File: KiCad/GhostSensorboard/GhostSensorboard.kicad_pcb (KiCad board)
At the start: 2 copper layers, 50 x 50 mm, 43 parts, among them P4 CONN_02X30, Q1 BSS138, Q2 BSS138, SW1 SW_Push, U1 TCA9548ARGER, U10 GP2Y0E02B, U11 GP2Y0E02B, U12 GP2Y0E02B, U13 INA219, U2 GP2Y0E02B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

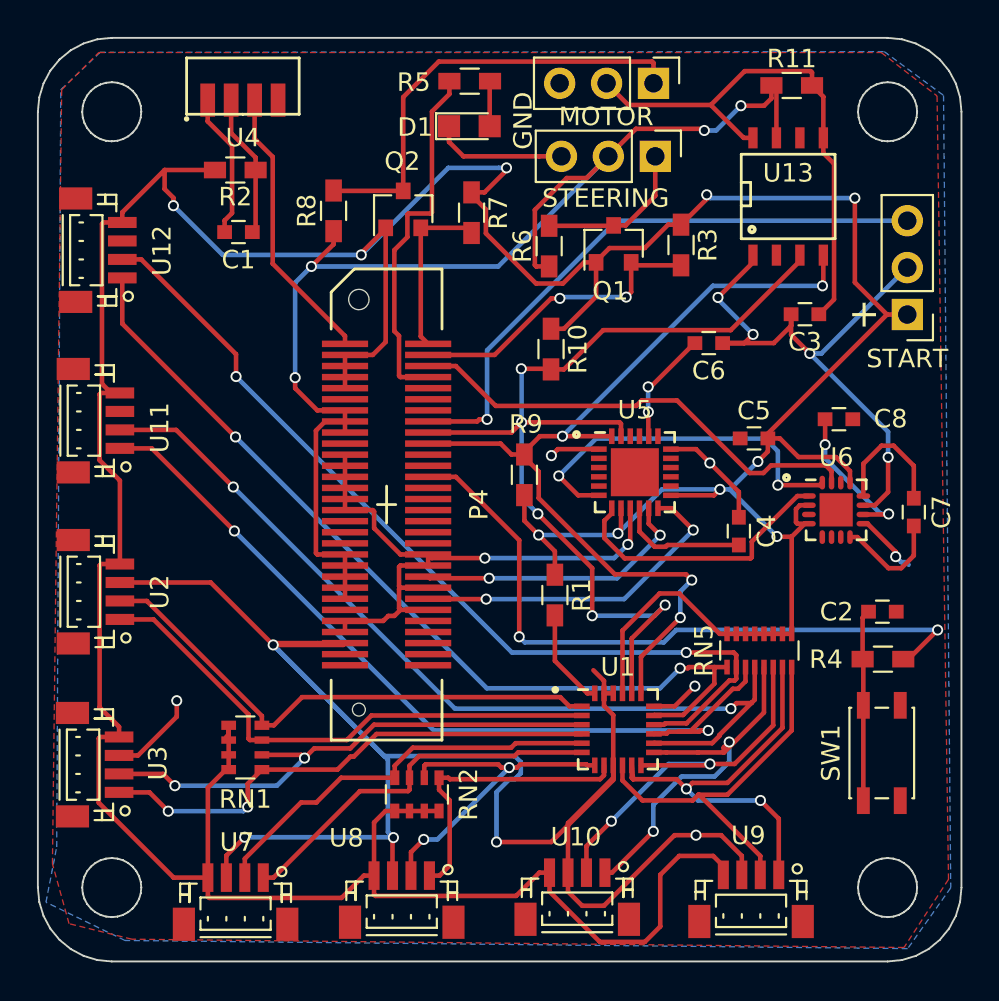
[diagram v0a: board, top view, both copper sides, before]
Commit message: Routing finished. Playing around with BOM as XSL file.
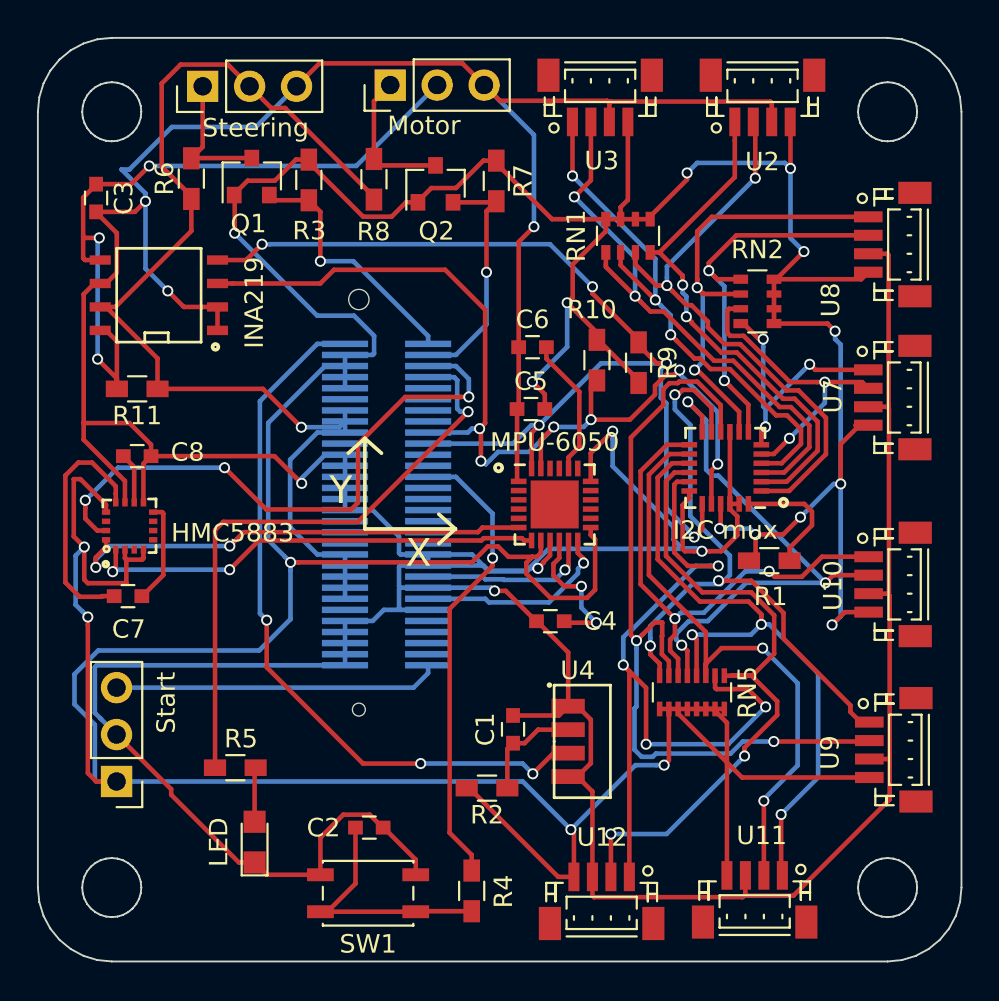
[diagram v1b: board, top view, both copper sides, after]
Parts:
- removed MOTOR: Motor, Pin_Headers:Pin_Header_Straight_1x03_Pitch2.54mm
- removed START: StartModule, Pin_Headers:Pin_Header_Straight_1x03_Pitch2.54mm
- removed STEERING: SteeringServo, Pin_Headers:Pin_Header_Straight_1x03_Pitch2.54mm
- removed U6: HMC5883, Housings_DFN_QFN:QFN-16-1EP_3x3mm_Pitch0.5mm
- added HMC5883: HMC5883, NorBotKiCadFootprints:HMC5883, F.Cu at (95.7, 101.6)
- added Motor: Motor, Pin_Headers:Pin_Header_Straight_1x03_Pitch2.54mm, F.Cu at (109.8, 77.7)
- added Start: StartModule, Pin_Headers:Pin_Header_Straight_1x03_Pitch2.54mm, F.Cu at (95.0, 115.4)
- added Steering: SteeringServo, Pin_Headers:Pin_Header_Straight_1x03_Pitch2.54mm, F.Cu at (99.7, 77.8)
- I2C mux: renamed from U1
- P4: footprint hrs-fx8c:hrs-fx8c-60p-sv -> hrs-fx8c:hrs-fx8c-60s-sv; moved to B.Cu
- moved U3 45.2 mm to (121.2, 78.4), turned to 0 degrees
- moved U2 44.9 mm to (130.0, 78.4), turned to 0 degrees
- moved U7 44.8 mm to (137.0, 94.6), turned to 270 degrees
- moved U12 44.5 mm to (121.3, 121.8), turned to 180 degrees
- moved U8 44.3 mm to (137.0, 86.3), turned to 270 degrees
- moved U11 44.0 mm to (129.5, 121.7), turned to 180 degrees
- moved C7 42.8 mm to (95.6, 105.4), turned to 0 degrees
- moved LED 40.5 mm to (102.5, 118.7), turned to 90 degrees
- moved U4 39.6 mm to (120.0, 113.2), turned to 270 degrees
- moved R5 39.3 mm to (101.4, 114.7)
- moved R11 39.1 mm to (96.1, 94.1), turned to 180 degrees
- moved C3 38.9 mm to (93.9, 83.8), turned to 270 degrees
- moved C8 38.0 mm to (96.1, 97.8)
- moved R2 36.1 mm to (115.1, 115.8)
- moved RN1 34.6 mm to (122.7, 85.9), turned to 90 degrees
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- renumbered U13 to INA219, D1 to LED, U5 to MPU-6050
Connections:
- P4 pad 31: Net-(P4-Pad31) -> GPIO_StartModule
- P4 pad 53: GPIO_StartModule -> Net-(P4-Pad53)
- P4 pad 59: GPIO_STEERING -> GPIO_MOTOR
- P4 pad 60: GPIO_MOTOR -> GPIO_STEERING
- RN1 pad 1: SC1 -> SD1
- RN1 pad 2: SD1 -> SC1
- RN1 pad 3: SC0 -> SD0
- RN1 pad 4: SD0 -> SC0
- RN2 pad 1: SC3 -> SD3
- RN2 pad 2: SD3 -> SC3
- RN2 pad 3: SC2 -> SD2
- RN2 pad 4: SD2 -> SC2
- RN5 pad 1: SC7 -> SD7
- RN5 pad 2: SD7 -> SC7
- RN5 pad 3: SC6 -> SD6
- RN5 pad 4: SD6 -> SC6
- RN5 pad 5: SC5 -> SD5
- RN5 pad 6: SD5 -> SC5
- RN5 pad 7: SC4 -> SD4
- RN5 pad 8: SD4 -> SC4
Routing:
- net GND: track 201.3 -> 309.0 mm, vias 16 -> 8
- net +3V3: track 249.0 -> 292.0 mm, vias 10 -> 17
- net GPIO_IR: track 15.2 -> 39.6 mm, vias 0 -> 3
- net SD4: track 21.2 -> 43.7 mm, vias 0 -> 2
- net MotorPWM: track 24.3 -> 7.84 mm
- net SD6: track 48.9 -> 32.7 mm
- net GPIO_StartModule: track 32.6 -> 17.6 mm, vias 1 -> 0
- net SD7: track 49.6 -> 36.0 mm
- net GPIO_LED: track 19.6 -> 33.1 mm, vias 0 -> 1
- net SC4: track 23.2 -> 35.7 mm, vias 2 -> 3
- net GPIO_BUTTON: track 37.1 -> 25.1 mm, vias 2 -> 1
- net SC6: track 46.7 -> 36.1 mm, vias 2 -> 3
- net +BATT: track 29.4 -> 39.2 mm, vias 0 -> 3
- net MPU_SCL: track 15.2 -> 24.7 mm, vias 0 -> 2
- net SC3: track 15.9 -> 24.4 mm, vias 0 -> 2
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- removed copper zone on B.Cu, net GND
- removed copper zone on F.Cu, net GND
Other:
- board text added: "Frode Lillerud 25.feb 2017"
- board text added: "X"
- board text added: "Y"
- board text removed: "+"
- board text removed: "Frode Lillerud 21.feb 2017"
- board text removed: "GND"

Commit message: Both boards done, and sent to Elecrow.
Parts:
- removed HMC5883: HMC5883, NorBotKiCadFootprints:HMC5883
- removed Start: StartModule, Pin_Headers:Pin_Header_Straight_1x03_Pitch2.54mm
- added P1: StartModule, Pin_Headers:Pin_Header_Straight_1x03_Pitch2.54mm, F.Cu at (95.1, 115.3)
- added U6: HMC5883, NorBotKiCadFootprints:HMC5883, F.Cu at (95.7, 101.5)
- U1: renamed from I2C mux
- renumbered LED to D1, Steering to P2, Motor to P3, INA219 to U13, MPU-6050 to U5
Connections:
- P4 pad 36: GND -> Net-(P4-Pad36)
- P4 pad 38: GND -> Net-(P4-Pad38)
- P4 pad 40: GND -> Net-(P4-Pad40)
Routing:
- net GND: track 309.0 -> 304.5 mm, vias 8 -> 9
- net GPIO_StartModule: track 17.6 -> 20.4 mm, vias 0 -> 2
- net Net-(C4-Pad2): track 7.86 -> 10.2 mm
- net GPIO_INT: track 10.9 -> 11.6 mm
- net SD6: track 32.7 -> 32.1 mm
- net +3V3: track 292.0 -> 292.6 mm
- added copper zone on B.Cu, net GND
- added copper zone on F.Cu, net GND

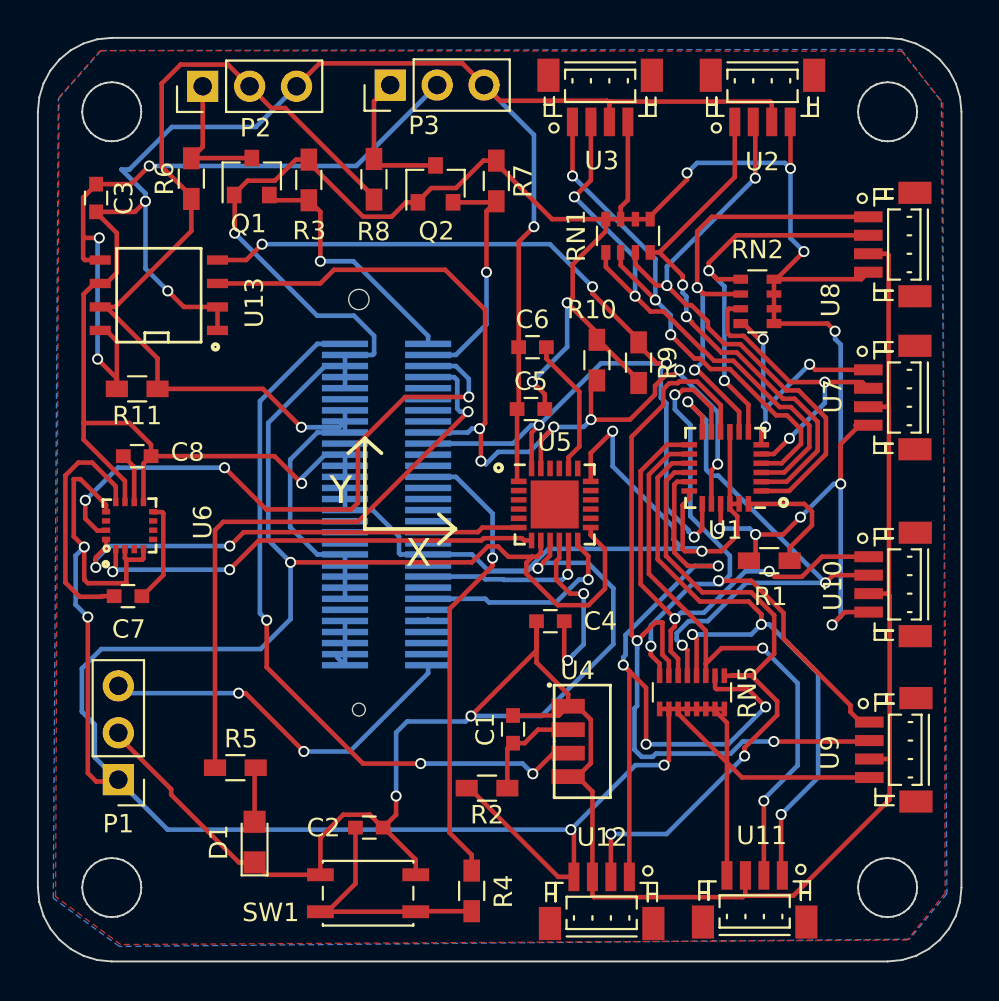
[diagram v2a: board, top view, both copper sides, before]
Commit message: Startmodule connected to GPIO instead of 3V3 for software power recycle. Motor-pwm connected to IO25 instead of IO34 (which is input only) DRDY connected to IO33 instead of IO35 (which is input only)
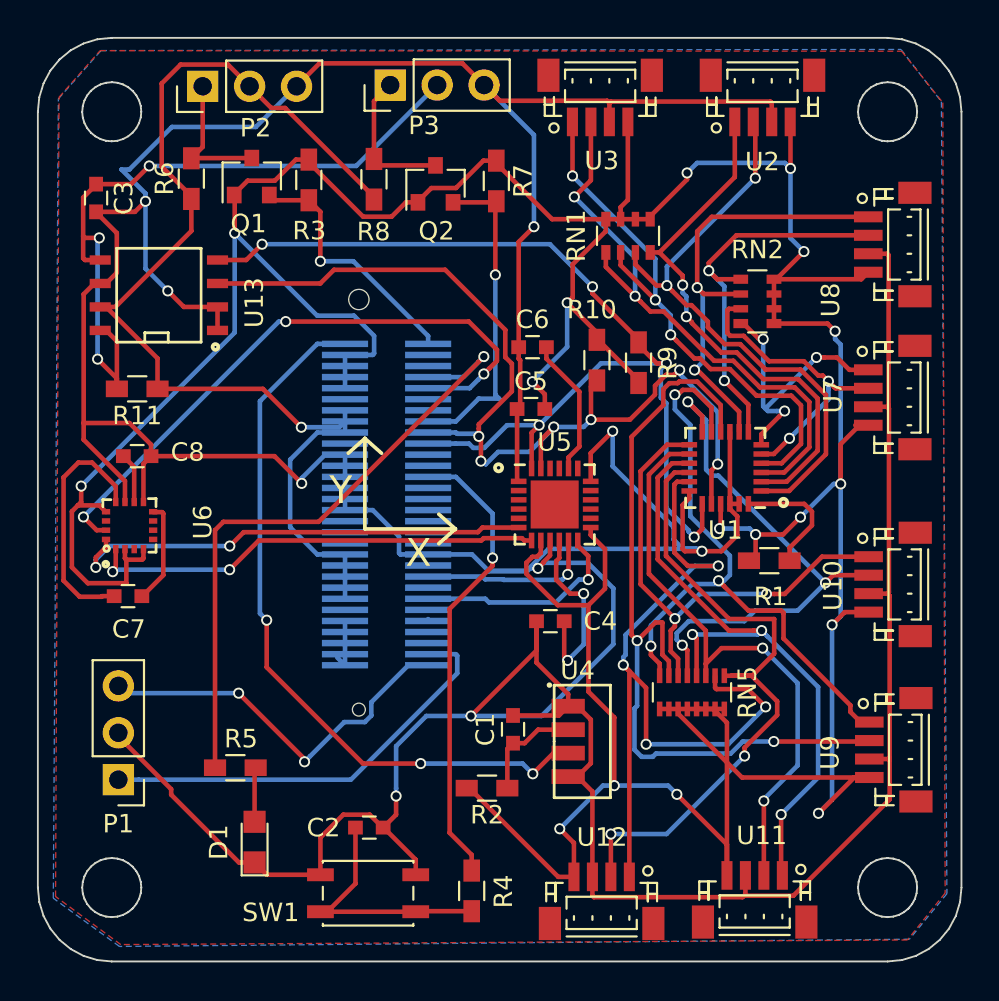
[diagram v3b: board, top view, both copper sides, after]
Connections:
- P1 pad 1: +3V3 -> GPIO_StartModule_VCC
- P4 pad 32: Net-(P4-Pad32) -> GPIO_StartModule_VCC
- P4 pad 53: Net-(P4-Pad53) -> GPIO_MOTOR
- P4 pad 56: Net-(P4-Pad56) -> GPIO_DRDY
- P4 pad 58: GPIO_DRDY -> Net-(P4-Pad58)
- P4 pad 59: GPIO_MOTOR -> Net-(P4-Pad59)
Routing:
- net +3V3: track 292.6 -> 247.5 mm
- net GPIO_StartModule_VCC: track 0.00 -> 23.3 mm
- net GPIO_MOTOR: track 13.1 -> 17.5 mm
- net GPIO_LED: track 33.1 -> 34.8 mm
- net SC2: track 14.1 -> 15.8 mm
- net GPIO_DRDY: track 32.7 -> 33.9 mm
- net GPIO_SDA: track 53.3 -> 54.5 mm
- net SC6: track 36.1 -> 35.2 mm
- net SC1: track 29.6 -> 30.4 mm
- net SD1: track 30.9 -> 31.6 mm
- net SC0: track 28.1 -> 28.9 mm
- net GPIO_StartModule: track 20.4 -> 21.1 mm
- net SD0: track 31.8 -> 32.5 mm
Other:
- board text added: "Frode Lillerud 27.feb 2017"
- board text removed: "Frode Lillerud 25.feb 2017"
